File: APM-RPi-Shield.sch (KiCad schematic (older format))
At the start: 31 parts, among them IC1 ADS1115, IC2 PCA9685, P1 CONN_13X2, P2 BMP180, P3 ADC, P4 SPI, P5 MPU9250, P6 I2C, P7 UART, P8 CONN_03X16

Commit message: fix on practic use
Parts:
- removed D1: 1N4148, Diodes_SMD:SOD-123, symbol D
- removed R1: 1K, Resistors_SMD:R_0805, symbol R
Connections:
- net GND: now also D2.1 (K), D3.1 (K), D4.1 (K); no longer D2.2 (A), D3.2 (A), D4.2 (A)
- net GPIO4(PPM): now also P8.35
- net at R6.1: now also D2.2 (A); no longer D2.1 (K)
- net at R7.1: now also D3.2 (A); no longer D3.1 (K)
- net at R8.1: now also D4.2 (A); no longer D4.1 (K)
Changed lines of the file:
@@
 BEC_5V
-$Comp
-L R R1
-U 1 1 554E213C
-P 2775 3725
-F 0 "R1" V 2855 3725 40  0000 C CNN
-F 1 "1K" V 2782 3726 40  0000 C CNN
-F 2 "Resistors_SMD:R_0805" V 2705 3725 30  0001 C CNN
-F 3 "~" H 2775 3725 30  0000 C CNN
-	1    2775 3725
-	0    -1   -1   0
-$EndComp
-$Comp
-L D D1
-U 1 1 554E213D
-P 3025 3325
-F 0 "D1" H 3025 3425 40  0000 C CNN
-F 1 "1N4148" H 3025 3225 40  0000 C CNN
-F 2 "Diodes_SMD:SOD-123" H 3025 3325 60  0001 C CNN
-F 3 "~" H 3025 3325 60  0000 C CNN
-	1    3025 3325
-	0    -1   -1   0
-$EndComp
-$Comp
-L +3.3V #PWR011
-U 1 1 554E213E
-P 3025 2975
-F 0 "#PWR011" H 3025 2935 30  0001 C CNN
-F 1 "+3.3V" H 3025 3085 30  0000 C CNN
-F 2 "" H 3025 2975 60  0000 C CNN
-F 3 "" H 3025 2975 60  0000 C CNN
-	1    3025 2975
-	1    0    0    -1
-$EndComp
 $Comp
 L PCA9685 IC2
@@
 $EndComp
 $Comp
-L GND #PWR012
+L GND #PWR011
 U 1 1 554E2140
 P 5975 4300
-F 0 "#PWR012" H 5975 4300 30  0001 C CNN
+F 0 "#PWR011" H 5975 4300 30  0001 C CNN
 F 1 "GND" H 5975 4230 30  0001 C CNN
 F 2 "" H 5975 4300 60  0000 C CNN
@@
 $EndComp
 $Comp
-L GND #PWR013
+L GND #PWR012
 U 1 1 554E2141
 P 7375 4225
-F 0 "#PWR013" H 7375 4225 30  0001 C CNN
+F 0 "#PWR012" H 7375 4225 30  0001 C CNN
 F 1 "GND" H 7375 4155 30  0001 C CNN
 F 2 "" H 7375 4225 60  0000 C CNN
@@
 F 3 "~" H 4025 5275 60  0000 C CNN
 	1    4025 5275
-	0    1    1    0
+	0    -1   -1   0
 $EndComp
 $Comp
@@
 F 3 "~" H 4425 5275 60  0000 C CNN
 	1    4425 5275
-	0    1    1    0
+	0    -1   -1   0
 $EndComp
 $Comp
@@
 F 3 "~" H 4825 5275 60  0000 C CNN
 	1    4825 5275
-	0    1    1    0
-$EndComp
-$Comp
-L GND #PWR014
+	0    -1   -1   0
+$EndComp
+$Comp
+L GND #PWR013
 U 1 1 554E2148
 P 4025 5575
-F 0 "#PWR014" H 4025 5575 30  0001 C CNN
+F 0 "#PWR013" H 4025 5575 30  0001 C CNN
 F 1 "GND" H 4025 5505 30  0001 C CNN
 F 2 "" H 4025 5575 60  0000 C CNN
@@
 $EndComp
 $Comp
-L GND #PWR015
+L GND #PWR014
 U 1 1 554E2149
 P 4425 5575
-F 0 "#PWR015" H 4425 5575 30  0001 C CNN
+F 0 "#PWR014" H 4425 5575 30  0001 C CNN
 F 1 "GND" H 4425 5505 30  0001 C CNN
 F 2 "" H 4425 5575 60  0000 C CNN
@@
 $EndComp
 $Comp
-L GND #PWR016
+L GND #PWR015
 U 1 1 554E214A
 P 4825 5575
-F 0 "#PWR016" H 4825 5575 30  0001 C CNN
+F 0 "#PWR015" H 4825 5575 30  0001 C CNN
 F 1 "GND" H 4825 5505 30  0001 C CNN
 F 2 "" H 4825 5575 60  0000 C CNN
@@
 SERVO_S13
 $Comp
-L GND #PWR017
+L GND #PWR016
 U 1 1 554E2158
 P 5975 5275
-F 0 "#PWR017" H 5975 5275 30  0001 C CNN
+F 0 "#PWR016" H 5975 5275 30  0001 C CNN
 F 1 "GND" H 5975 5205 30  0001 C CNN
 F 2 "" H 5975 5275 60  0000 C CNN
@@
 $EndComp
 $Comp
-L +3.3V #PWR018
+L +3.3V #PWR017
 U 1 1 554E2159
 P 7275 3825
-F 0 "#PWR018" H 7275 3785 30  0001 C CNN
+F 0 "#PWR017" H 7275 3785 30  0001 C CNN
 F 1 "+3.3V" H 7275 3935 30  0000 C CNN
 F 2 "" H 7275 3825 60  0000 C CNN
@@
 $EndComp
 $Comp
-L GND #PWR019
+L GND #PWR018
 U 1 1 554E215B
 P 9600 3100
-F 0 "#PWR019" H 9600 3100 30  0001 C CNN
+F 0 "#PWR018" H 9600 3100 30  0001 C CNN
 F 1 "GND" H 9600 3030 30  0001 C CNN
 F 2 "" H 9600 3100 60  0000 C CNN
@@
 $EndComp
 $Comp
-L GND #PWR020
+L GND #PWR019
 U 1 1 554E215D
 P 6750 1200
-F 0 "#PWR020" H 6750 1200 30  0001 C CNN
+F 0 "#PWR019" H 6750 1200 30  0001 C CNN
 F 1 "GND" H 6750 1130 30  0001 C CNN
 F 2 "" H 6750 1200 60  0000 C CNN
@@
 NoConn ~ 7100 950
 $Comp
-L +3.3V #PWR021
+L +3.3V #PWR020
 U 1 1 554E215E
 P 9025 1050
-F 0 "#PWR021" H 9025 1010 30  0001 C CNN
+F 0 "#PWR020" H 9025 1010 30  0001 C CNN
 F 1 "+3.3V" H 9025 1160 30  0000 C CNN
 F 2 "" H 9025 1050 60  0000 C CNN
@@
 $EndComp
 $Comp
-L +3.3V #PWR022
+L +3.3V #PWR021
 U 1 1 554E2160
 P 8400 1500
-F 0 "#PWR022" H 8400 1460 30  0001 C CNN
+F 0 "#PWR021" H 8400 1460 30  0001 C CNN
 F 1 "+3.3V" H 8400 1610 30  0000 C CNN
 F 2 "" H 8400 1500 60  0000 C CNN
@@
 $EndComp
 $Comp
-L GND #PWR023
+L GND #PWR022
 U 1 1 554E2161
 P 8400 2175
-F 0 "#PWR023" H 8400 2175 30  0001 C CNN
+F 0 "#PWR022" H 8400 2175 30  0001 C CNN
 F 1 "GND" H 8400 2105 30  0001 C CNN
 F 2 "" H 8400 2175 60  0000 C CNN
@@
 BEC_5V
 $Comp
-L GND #PWR024
+L GND #PWR023
 U 1 1 554E2163
 P 8425 3300
-F 0 "#PWR024" H 8425 3300 30  0001 C CNN
+F 0 "#PWR023" H 8425 3300 30  0001 C CNN
 F 1 "GND" H 8425 3230 30  0001 C CNN
 F 2 "" H 8425 3300 60  0000 C CNN
@@
 $EndComp
 $Comp
-L GND #PWR025
+L GND #PWR024
 U 1 1 554E2165
 P 9600 2375
-F 0 "#PWR025" H 9600 2375 30  0001 C CNN
+F 0 "#PWR024" H 9600 2375 30  0001 C CNN
 F 1 "GND" H 9600 2305 30  0001 C CNN
 F 2 "" H 9600 2375 60  0000 C CNN
@@
 GPIO1(SCL)
 $Comp
-L GND #PWR026
+L GND #PWR025
 U 1 1 554E5FA9
 P 2800 1600
-F 0 "#PWR026" H 2800 1600 30  0001 C CNN
+F 0 "#PWR025" H 2800 1600 30  0001 C CNN
 F 1 "GND" H 2800 1530 30  0001 C CNN
 F 2 "" H 2800 1600 60  0001 C CNN
@@
 $EndComp
 $Comp
-L GND #PWR027
+L GND #PWR026
 U 1 1 554E61B2
 P 3625 1400
-F 0 "#PWR027" H 3625 1400 30  0001 C CNN
+F 0 "#PWR026" H 3625 1400 30  0001 C CNN
 F 1 "GND" H 3625 1330 30  0001 C CNN
 F 2 "" H 3625 1400 60  0001 C CNN
@@
 $EndComp
 $Comp
-L GND #PWR028
+L GND #PWR027
 U 1 1 554E6495
 P 3625 1800
-F 0 "#PWR028" H 3625 1800 30  0001 C CNN
+F 0 "#PWR027" H 3625 1800 30  0001 C CNN
 F 1 "GND" H 3625 1730 30  0001 C CNN
 F 2 "" H 3625 1800 60  0001 C CNN
@@
 $EndComp
 $Comp
-L +3.3V #PWR029
+L +3.3V #PWR028
 U 1 1 554E667F
 P 2800 2050
-F 0 "#PWR029" H 2800 2010 30  0001 C CNN
+F 0 "#PWR028" H 2800 2010 30  0001 C CNN
 F 1 "+3.3V" H 2850 2125 30  0000 C CNN
 F 2 "" H 2800 2050 60  0001 C CNN
@@
 $EndComp
 $Comp
-L GND #PWR030
+L GND #PWR029
 U 1 1 554E6893
 P 3625 2100
-F 0 "#PWR030" H 3625 2100 30  0001 C CNN
+F 0 "#PWR029" H 3625 2100 30  0001 C CNN
 F 1 "GND" H 3625 2030 30  0001 C CNN
 F 2 "" H 3625 2100 60  0001 C CNN
@@
 $EndComp
 $Comp
-L GND #PWR031
+L GND #PWR030
 U 1 1 554E6A63
 P 2850 2475
-F 0 "#PWR031" H 2850 2475 30  0001 C CNN
+F 0 "#PWR030" H 2850 2475 30  0001 C CNN
 F 1 "GND" H 2850 2405 30  0001 C CNN
 F 2 "" H 2850 2475 60  0001 C CNN
@@
 Connection ~ 1750 4675
 Wire Wire Line
-	2925 3725 3125 3725
-Wire Wire Line
-	3025 3725 3025 3475
-Connection ~ 3025 3725
-Wire Wire Line
-	3025 3175 3025 2975
+	2600 3725 3125 3725
 Wire Wire Line
 	5975 4225 6175 4225
@@
 Wire Wire Line
 	2600 3775 2600 3725
-Wire Wire Line
-	2600 3725 2625 3725
 Wire Wire Line
 	2175 1525 2925 1525
@@
 NoConn ~ 2175 1925
 $Comp
-L +5V #PWR032
+L +5V #PWR031
 U 1 1 554EEB19
 P 1675 3425
-F 0 "#PWR032" H 1675 3515 20  0001 C CNN
+F 0 "#PWR031" H 1675 3515 20  0001 C CNN
 F 1 "+5V" H 1675 3550 30  0000 C CNN
 F 2 "" H 1675 3425 60  0001 C CNN
@@
 $EndComp
 $Comp
-L PWR_FLAG #FLG033
+L PWR_FLAG #FLG032
 U 1 1 554EF261
 P 700 800
-F 0 "#FLG033" H 700 895 50  0001 C CNN
+F 0 "#FLG032" H 700 895 50  0001 C CNN
 F 1 "PWR_FLAG" H 700 980 50  0000 C CNN
 F 2 "" H 700 800 60  0000 C CNN
@@
 $EndComp
 $Comp
-L PWR_FLAG #FLG034
+L PWR_FLAG #FLG033
 U 1 1 554EF294
 P 1075 800
-F 0 "#FLG034" H 1075 895 50  0001 C CNN
+F 0 "#FLG033" H 1075 895 50  0001 C CNN
 F 1 "PWR_FLAG" H 1075 980 50  0000 C CNN
 F 2 "" H 1075 800 60  0000 C CNN
@@
 $EndComp
 $Comp
-L PWR_FLAG #FLG035
+L PWR_FLAG #FLG034
 U 1 1 554EF2C7
 P 1450 800
-F 0 "#FLG035" H 1450 895 50  0001 C CNN
+F 0 "#FLG034" H 1450 895 50  0001 C CNN
 F 1 "PWR_FLAG" H 1450 980 50  0000 C CNN
 F 2 "" H 1450 800 60  0000 C CNN
@@
 	1675 3575 1650 3575
 $Comp
-L GND #PWR036
+L GND #PWR035
 U 1 1 554F0BFF
 P 950 5100
-F 0 "#PWR036" H 950 5100 30  0001 C CNN
+F 0 "#PWR035" H 950 5100 30  0001 C CNN
 F 1 "GND" H 950 5030 30  0001 C CNN
 F 2 "" H 950 5100 60  0000 C CNN
@@
 $EndComp
 Wire Wire Line
-	1050 5075 950  5075
+	950  5075 1050 5075
 Wire Wire Line
 	950  3575 950  5100
@@
 Connection ~ 1750 3675
 $Comp
-L PWR_FLAG #FLG037
+L PWR_FLAG #FLG036
 U 1 1 554E388D
 P 1850 800
-F 0 "#FLG037" H 1850 895 50  0001 C CNN
+F 0 "#FLG036" H 1850 895 50  0001 C CNN
 F 1 "PWR_FLAG" H 1850 980 50  0000 C CNN
 F 2 "" H 1850 800 60  0000 C CNN

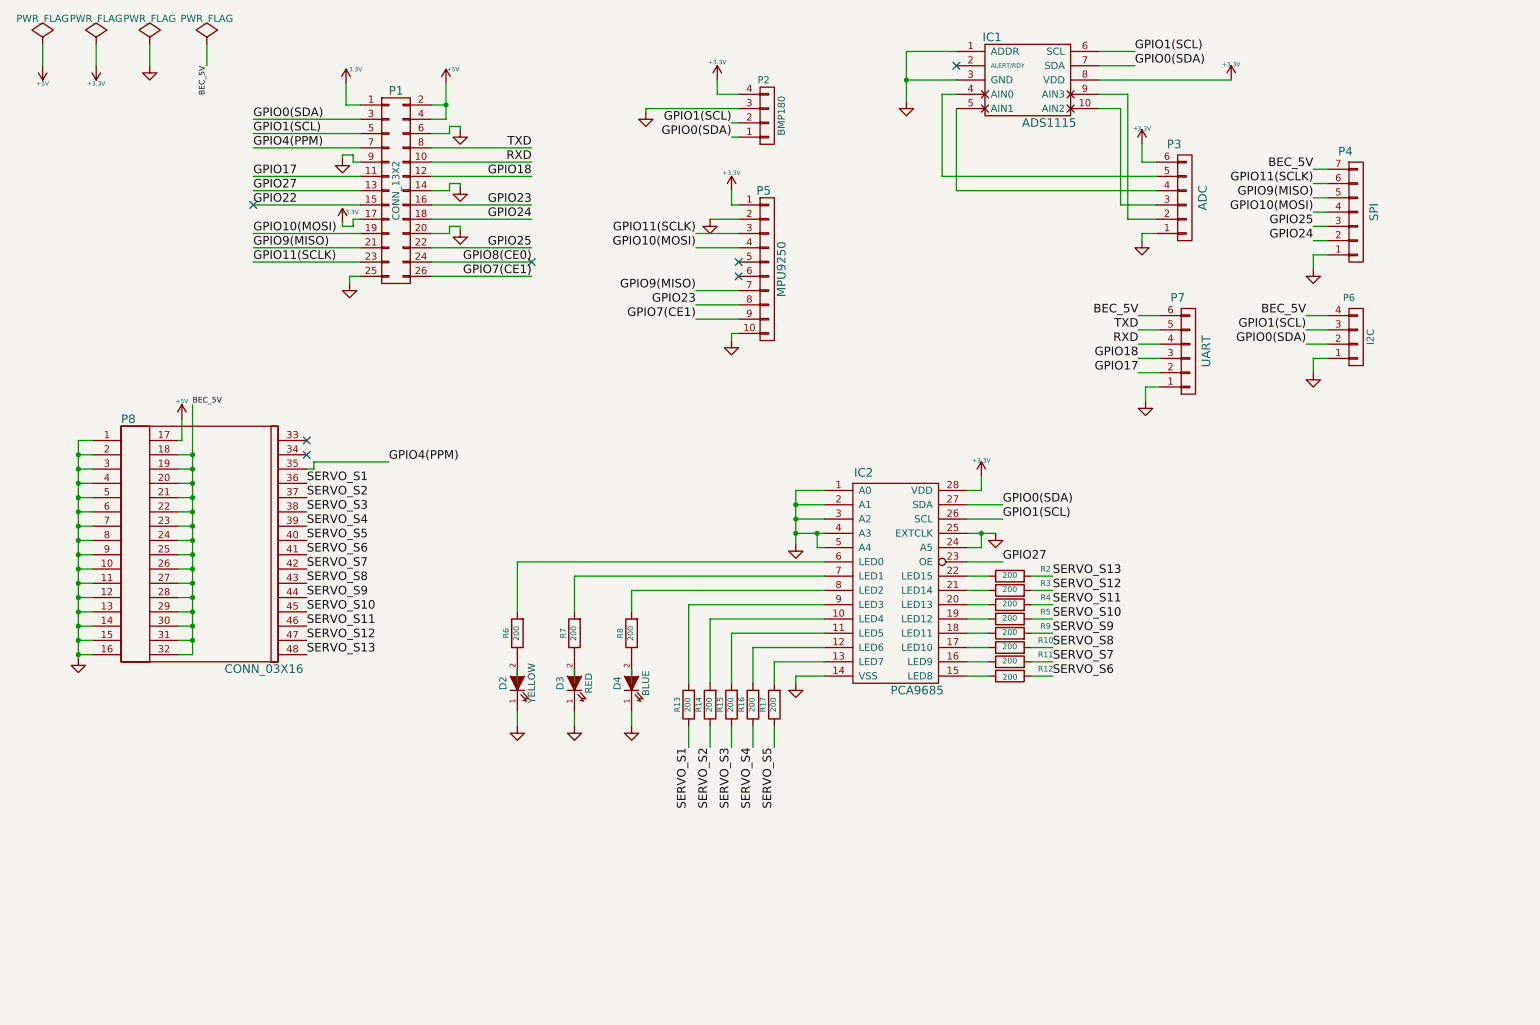
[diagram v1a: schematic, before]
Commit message: Add ublox GPS
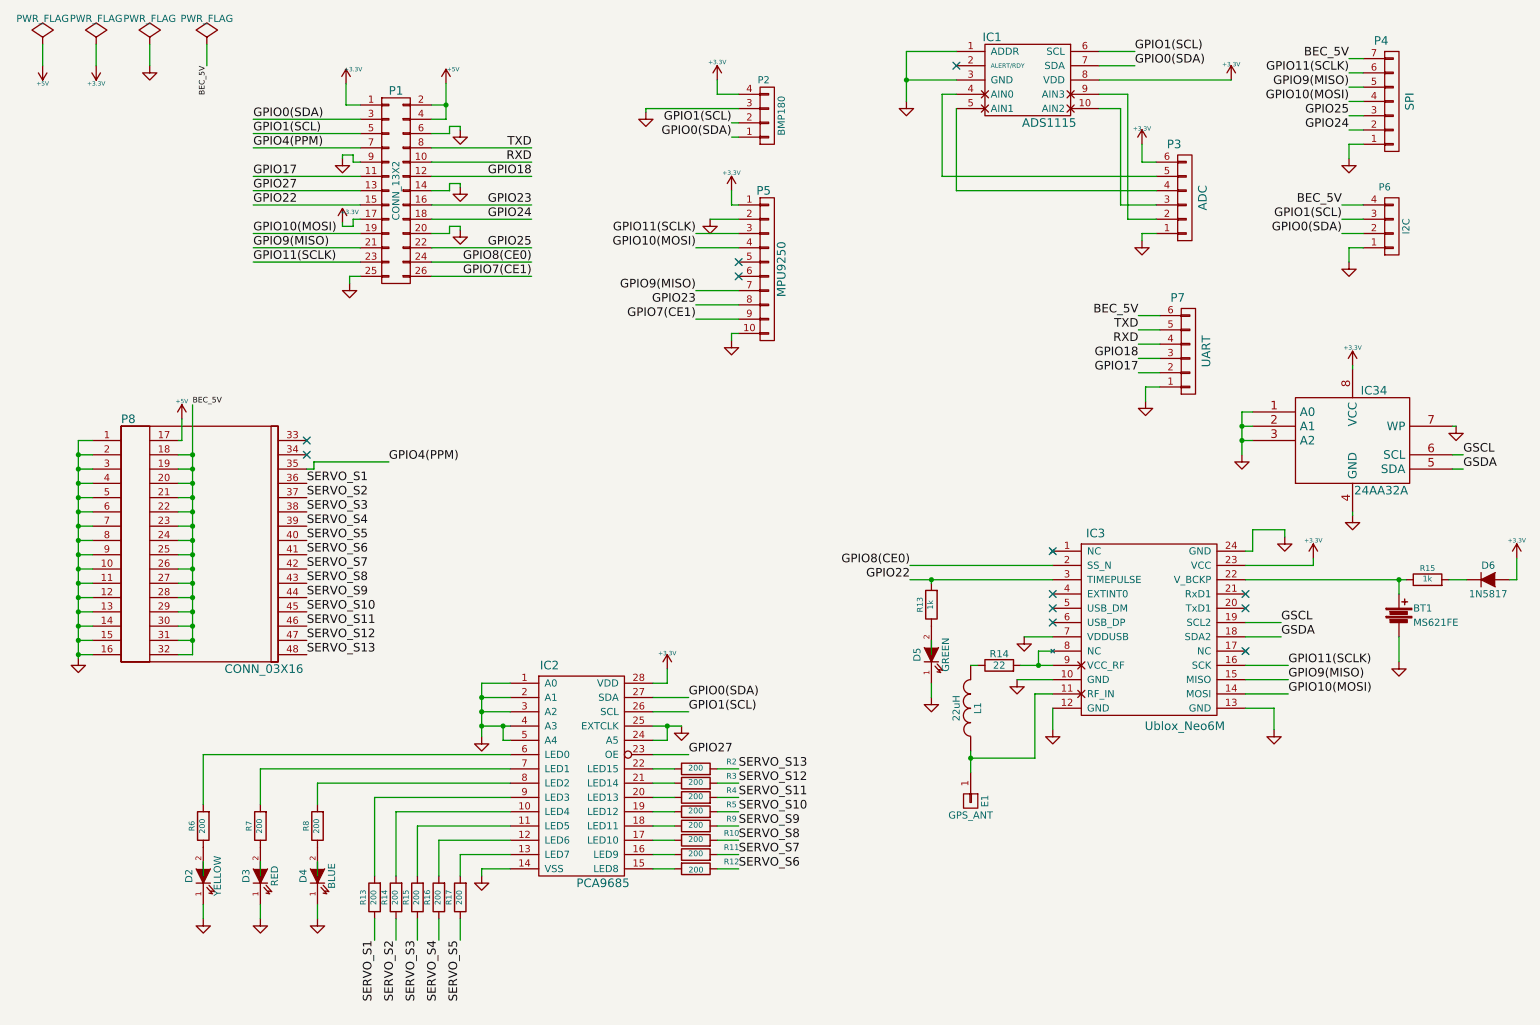
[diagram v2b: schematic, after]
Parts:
- added BT1: MS621FE, symbol Battery
- added D5: GREEN, LEDs:LED-3MM, symbol LED
- added D6: 1N5817, symbol D
- added E1: GPS_ANT, symbol CONN_01X01
- added IC3: Ublox_Neo6M, symbol Ublox_Neo6M
- added IC34: 24AA32A, symbol 24C512
- added L1: 22uH, symbol INDUCTOR
- added R13, R15: 1k, Resistors_SMD:R_0805, symbol R
- added R14: 22, symbol R
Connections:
- net +3V3: now also D6.2 (A), IC3.23 (VCC), IC34.8 (VCC)
- net GND: now also BT1.2, D5.1 (K), IC3.10 (GND), IC3.12 (GND), IC3.13 (GND), IC3.24 (GND), IC3.7 (VDDUSB), IC34.1 (A0), IC34.2 (A1), IC34.3 (A2), IC34.4 (GND), IC34.7 (WP)
- net GPIO10(MOSI): now also IC3.14 (MOSI)
- net GPIO11(SCLK): now also IC3.16 (SCK)
- net GPIO22: now also IC3.3 (TIMEPULSE), R13.2
- net GPIO8(CE0): now also IC3.2 (SS_N)
- net GPIO9(MISO): now also IC3.15 (MISO)
- new net: E1.1 (P1), IC3.11 (RF_IN), L1.1
- new net: BT1.1, IC3.22 (V_BCKP), R15.1
- new net: IC3.8 (NC), IC3.9 (VCC_RF), R14.2
- new net: D5.2 (A), R13.1
- new net: L1.2, R14.1
- new net: D6.1 (K), R15.2
- new net GSCL: IC3.19 (SCL2), IC34.6 (SCL)
- new net GSDA: IC3.18 (SDA2), IC34.5 (SDA)
- no-connect marks 7 -> 12
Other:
- moved on the sheet: D2, D3, D4, IC2, P4, P6, R10, R11, R12, R13, R14, R15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
